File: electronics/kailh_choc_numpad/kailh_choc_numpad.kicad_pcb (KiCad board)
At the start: 2 copper layers, 10 x 10 mm, 18 parts

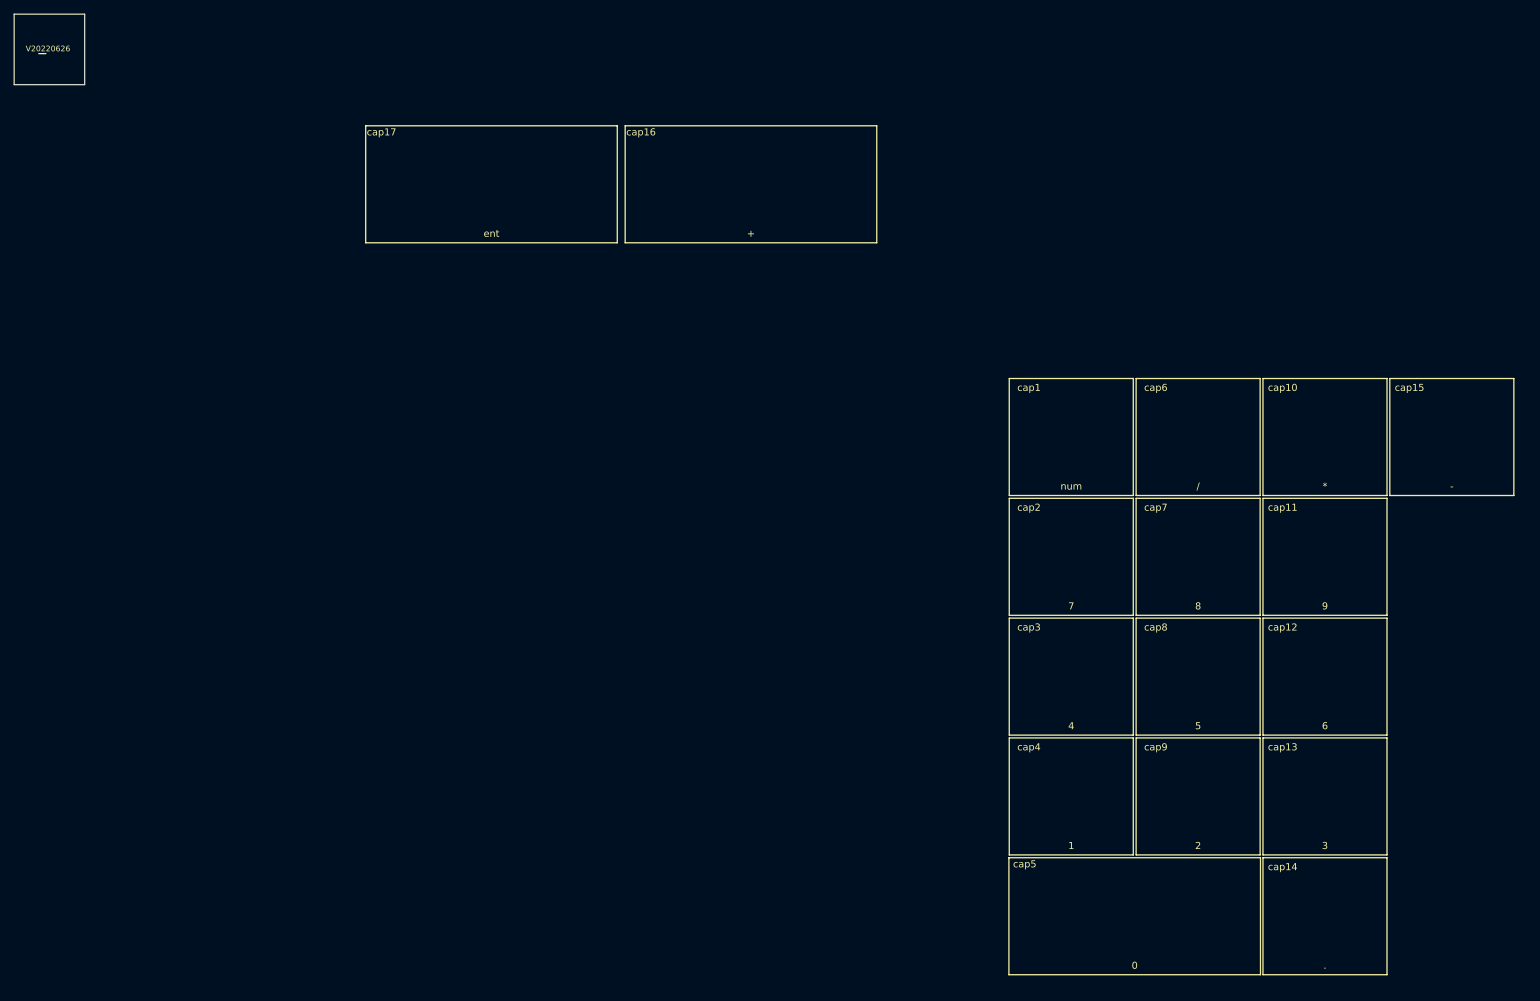
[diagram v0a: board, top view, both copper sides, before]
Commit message: placed keycaps
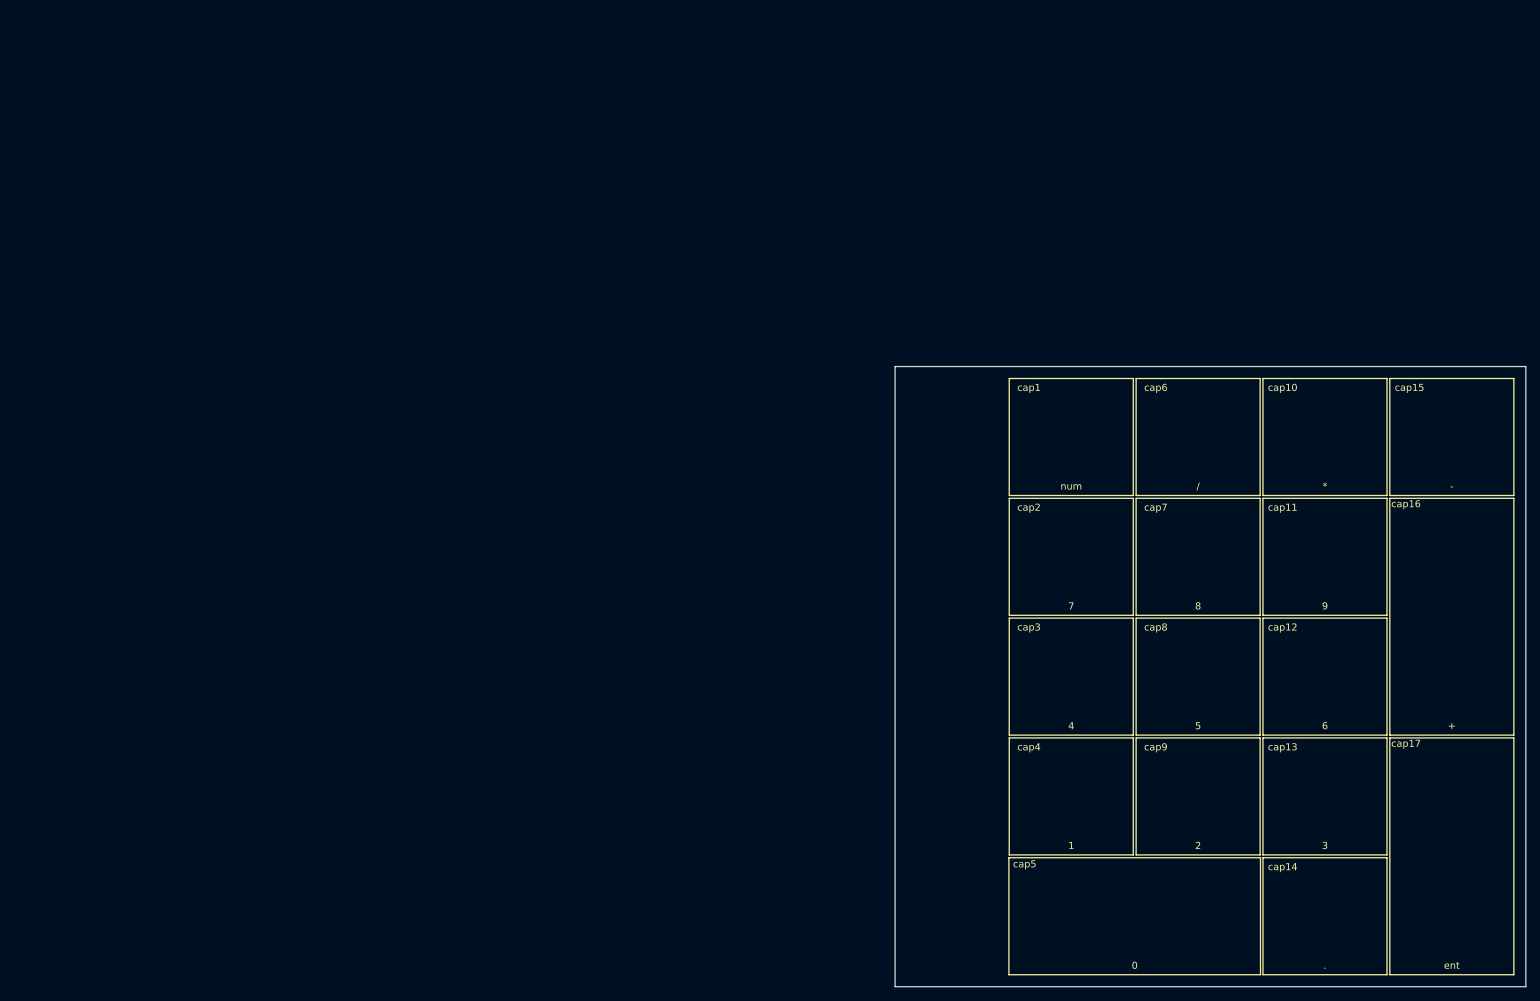
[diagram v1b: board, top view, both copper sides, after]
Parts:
- N1: moved to B.Cu
- cap16, cap17: footprint SquantorSwitches:KAILH_choc_keycap_2 -> SquantorSwitches:KAILH_choc_keycap_2_vertical
- cap5: footprint SquantorSwitches:KAILH_choc_keycap_2 -> SquantorSwitches:KAILH_choc_keycap_2_horizontal
- moved N1 227.3 mm to (224.5, 132.0), turned to 180 degrees
- moved cap17 166.3 mm to (224.0, 139.5)
- moved cap16 116.9 mm to (224.0, 105.5)
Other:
- board size 10 x 10 mm -> 89.5 x 88 mm

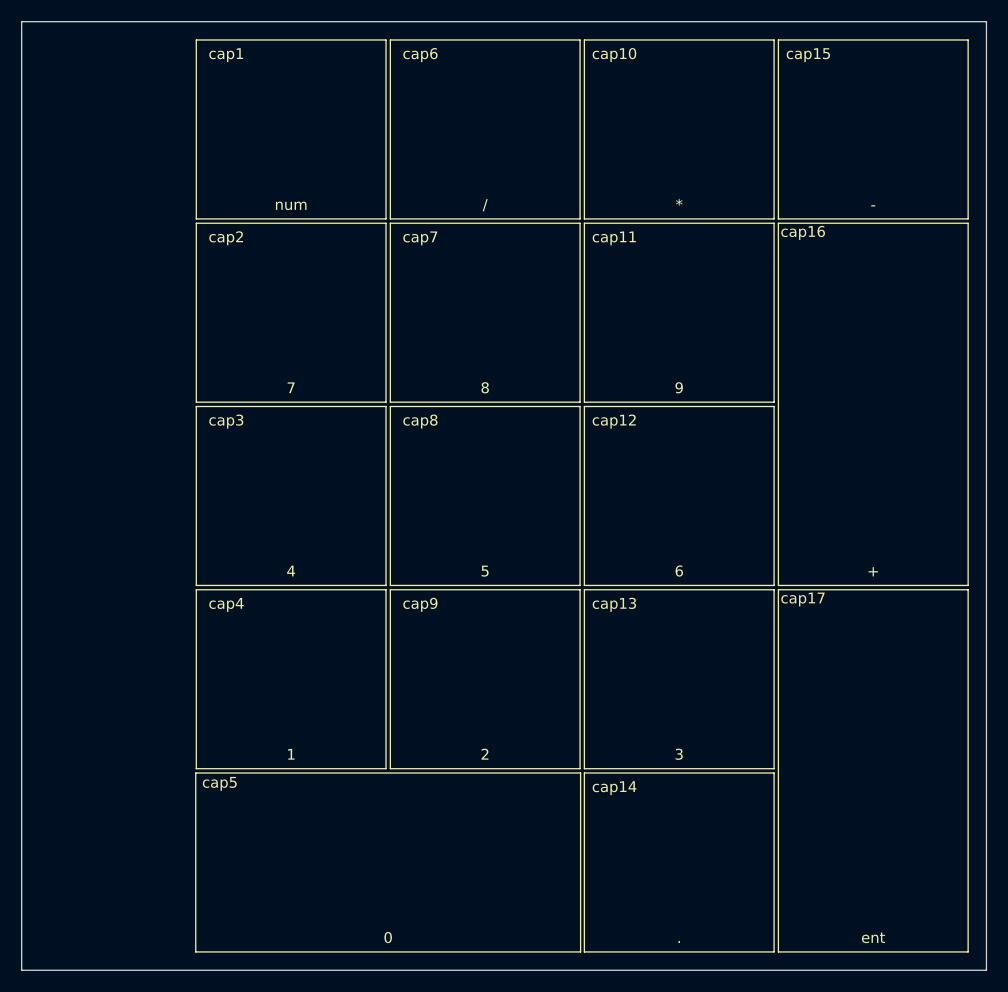
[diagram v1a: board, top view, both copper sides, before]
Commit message: placing and routing keyboard matrix
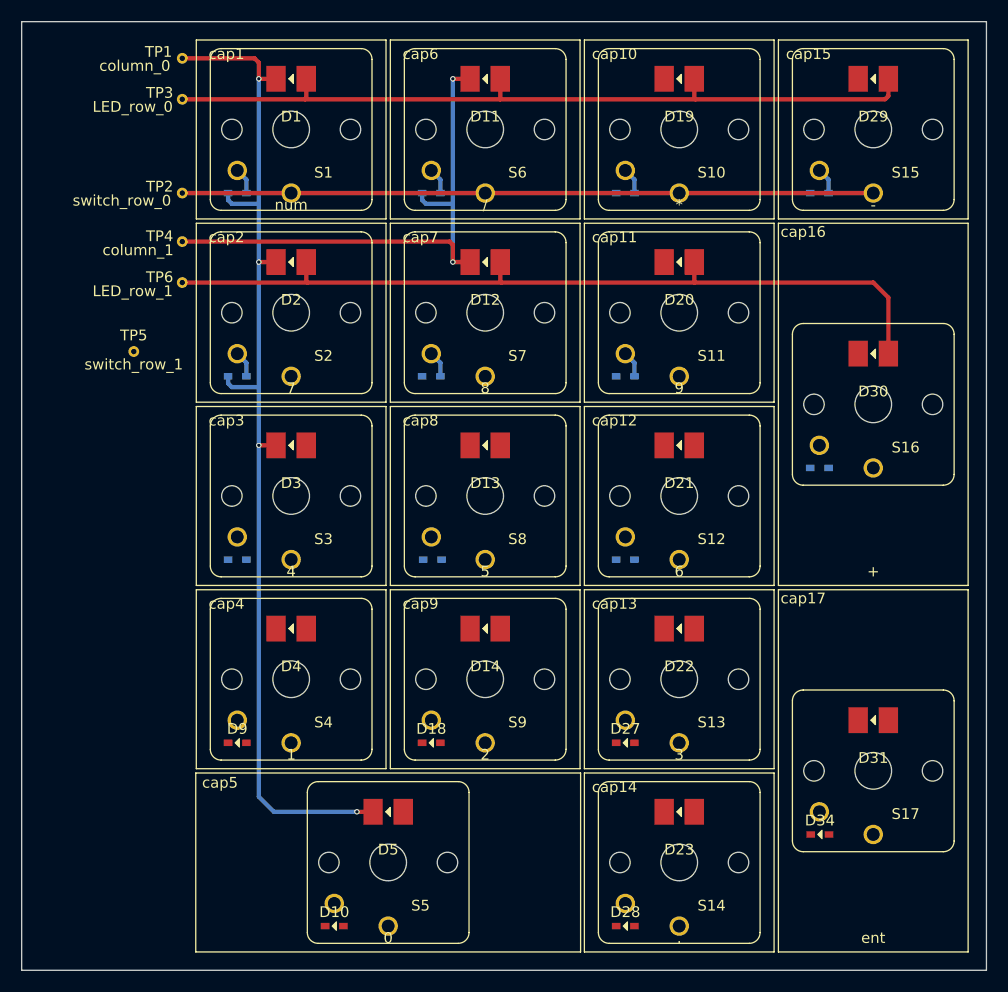
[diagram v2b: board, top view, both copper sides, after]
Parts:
- added D1: num, SquantorDiodes:LED_1208_0603, F.Cu at (170.0, 75.3)
- added D10: D, SquantorDiodes:SOD-523_hand, F.Cu at (174.0, 153.9)
- added D11: /, SquantorDiodes:LED_1208_0603, F.Cu at (188.0, 75.3)
- added D12: 8, SquantorDiodes:LED_1208_0603, F.Cu at (188.0, 92.3)
- added D13: 5, SquantorDiodes:LED_1208_0603, F.Cu at (188.0, 109.3)
- added D14: 2, SquantorDiodes:LED_1208_0603, F.Cu at (188.0, 126.3)
- added D15: D, SquantorDiodes:SOD-523_hand, B.Cu at (183.0, 85.9)
- added D16: D, SquantorDiodes:SOD-523_hand, B.Cu at (183.0, 102.9)
- added D17: D, SquantorDiodes:SOD-523_hand, B.Cu at (183.1, 119.9)
- added D18: D, SquantorDiodes:SOD-523_hand, F.Cu at (183.0, 136.9)
- added D19: *, SquantorDiodes:LED_1208_0603, F.Cu at (206.0, 75.3)
- added D2: 7, SquantorDiodes:LED_1208_0603, F.Cu at (170.0, 92.3)
- added D20: 9, SquantorDiodes:LED_1208_0603, F.Cu at (206.0, 92.3)
- added D21: 6, SquantorDiodes:LED_1208_0603, F.Cu at (206.0, 109.3)
- added D22: 3, SquantorDiodes:LED_1208_0603, F.Cu at (206.0, 126.3)
- added D23: ., SquantorDiodes:LED_1208_0603, F.Cu at (206.0, 143.3)
- added D24: D, SquantorDiodes:SOD-523_hand, B.Cu at (201.0, 85.9)
- added D25: D, SquantorDiodes:SOD-523_hand, B.Cu at (201.0, 102.9)
- added D26: D, SquantorDiodes:SOD-523_hand, B.Cu at (201.0, 119.9)
- added D27: D, SquantorDiodes:SOD-523_hand, F.Cu at (201.0, 136.9)
- added D28: D, SquantorDiodes:SOD-523_hand, F.Cu at (201.0, 153.9)
- added D29: -, SquantorDiodes:LED_1208_0603, F.Cu at (224.0, 75.3)
- added D3: 4, SquantorDiodes:LED_1208_0603, F.Cu at (170.0, 109.3)
- added D30: +, SquantorDiodes:LED_1208_0603, F.Cu at (224.0, 100.8)
- added D31: ent, SquantorDiodes:LED_1208_0603, F.Cu at (224.0, 134.8)
- added D32: D, SquantorDiodes:SOD-523_hand, B.Cu at (219.0, 85.9)
- added D33: D, SquantorDiodes:SOD-523_hand, B.Cu at (219.0, 111.4)
- added D34: D, SquantorDiodes:SOD-523_hand, F.Cu at (219.1, 145.4)
- added D4: 1, SquantorDiodes:LED_1208_0603, F.Cu at (170.0, 126.3)
- added D5: 0, SquantorDiodes:LED_1208_0603, F.Cu at (179.0, 143.3)
- added D6: D, SquantorDiodes:SOD-523_hand, B.Cu at (165.0, 85.9)
- added D7: D, SquantorDiodes:SOD-523_hand, B.Cu at (165.0, 102.9)
- added D8: D, SquantorDiodes:SOD-523_hand, B.Cu at (165.0, 119.9)
- added D9: D, SquantorDiodes:SOD-523_hand, F.Cu at (165.0, 136.9)
- added S1: num, SquantorSwitches:KAILH_choc_LED, F.Cu at (170.0, 80.0)
- added S10: *, SquantorSwitches:KAILH_choc_LED, F.Cu at (206.0, 80.0)
- added S11: 9, SquantorSwitches:KAILH_choc_LED, F.Cu at (206.0, 97.0)
- added S12: 6, SquantorSwitches:KAILH_choc_LED, F.Cu at (206.0, 114.0)
- added S13: 3, SquantorSwitches:KAILH_choc_LED, F.Cu at (206.0, 131.0)
- added S14: ., SquantorSwitches:KAILH_choc_LED, F.Cu at (206.0, 148.0)
- added S15: -, SquantorSwitches:KAILH_choc_LED, F.Cu at (224.0, 80.0)
- added S16: +, SquantorSwitches:KAILH_choc_LED, F.Cu at (224.0, 105.5)
- added S17: ent, SquantorSwitches:KAILH_choc_LED, F.Cu at (224.0, 139.5)
- added S2: 7, SquantorSwitches:KAILH_choc_LED, F.Cu at (170.0, 97.0)
- added S3: 4, SquantorSwitches:KAILH_choc_LED, F.Cu at (170.0, 114.0)
- added S4: 1, SquantorSwitches:KAILH_choc_LED, F.Cu at (170.0, 131.0)
- added S5: 0, SquantorSwitches:KAILH_choc_LED, F.Cu at (179.0, 148.0)
- added S6: /, SquantorSwitches:KAILH_choc_LED, F.Cu at (188.0, 80.0)
- added S7: 8, SquantorSwitches:KAILH_choc_LED, F.Cu at (188.0, 97.0)
- added S8: 5, SquantorSwitches:KAILH_choc_LED, F.Cu at (188.0, 114.0)
- added S9: 2, SquantorSwitches:KAILH_choc_LED, F.Cu at (188.0, 131.0)
- added TP1: column_0, SquantorTestPoints:TestPoint_hole_H05R10, F.Cu at (159.9, 73.4)
- added TP2: switch_row_0, SquantorTestPoints:TestPoint_hole_H05R10, F.Cu at (159.9, 85.9)
- added TP3: LED_row_0, SquantorTestPoints:TestPoint_hole_H05R10, F.Cu at (159.9, 77.2)
- added TP4: column_1, SquantorTestPoints:TestPoint_hole_H05R10, F.Cu at (159.9, 90.4)
- added TP5: switch_row_1, SquantorTestPoints:TestPoint_hole_H05R10, F.Cu at (155.4, 100.6)
- added TP6: LED_row_1, SquantorTestPoints:TestPoint_hole_H05R10, F.Cu at (159.9, 94.2)
- moved N1 75.1 mm to (153.0, 155.0)
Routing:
- net /column_0: track 0.00 -> 98.6 mm, vias 0 -> 4
- net /LED_row_1: track 0.00 -> 77.1 mm
- net /LED_row_0: track 0.00 -> 73.0 mm
- net /switch_row_0: track 0.00 -> 64.1 mm
- net /column_1: track 0.00 -> 50.7 mm, vias 0 -> 2
- net Net-(D7-Pad2): track 0.00 -> 2.45 mm
- net Net-(D6-Pad2): track 0.00 -> 2.45 mm
- net Net-(D32-Pad2): track 0.00 -> 2.45 mm
- net Net-(D25-Pad2): track 0.00 -> 2.45 mm
- net Net-(D24-Pad2): track 0.00 -> 2.45 mm
- net Net-(D16-Pad2): track 0.00 -> 2.45 mm
- net Net-(D15-Pad2): track 0.00 -> 2.45 mm

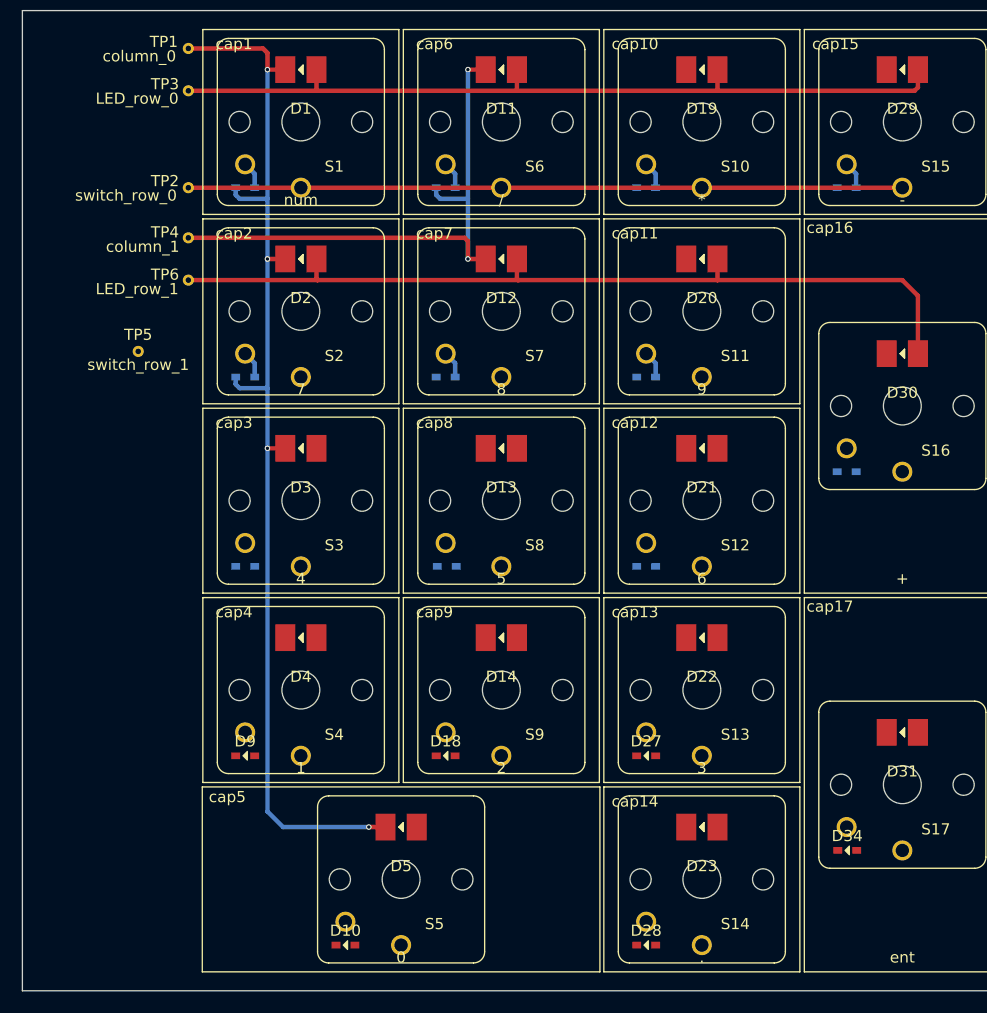
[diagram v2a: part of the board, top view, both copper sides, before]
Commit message: fully placed and routed switch matrix
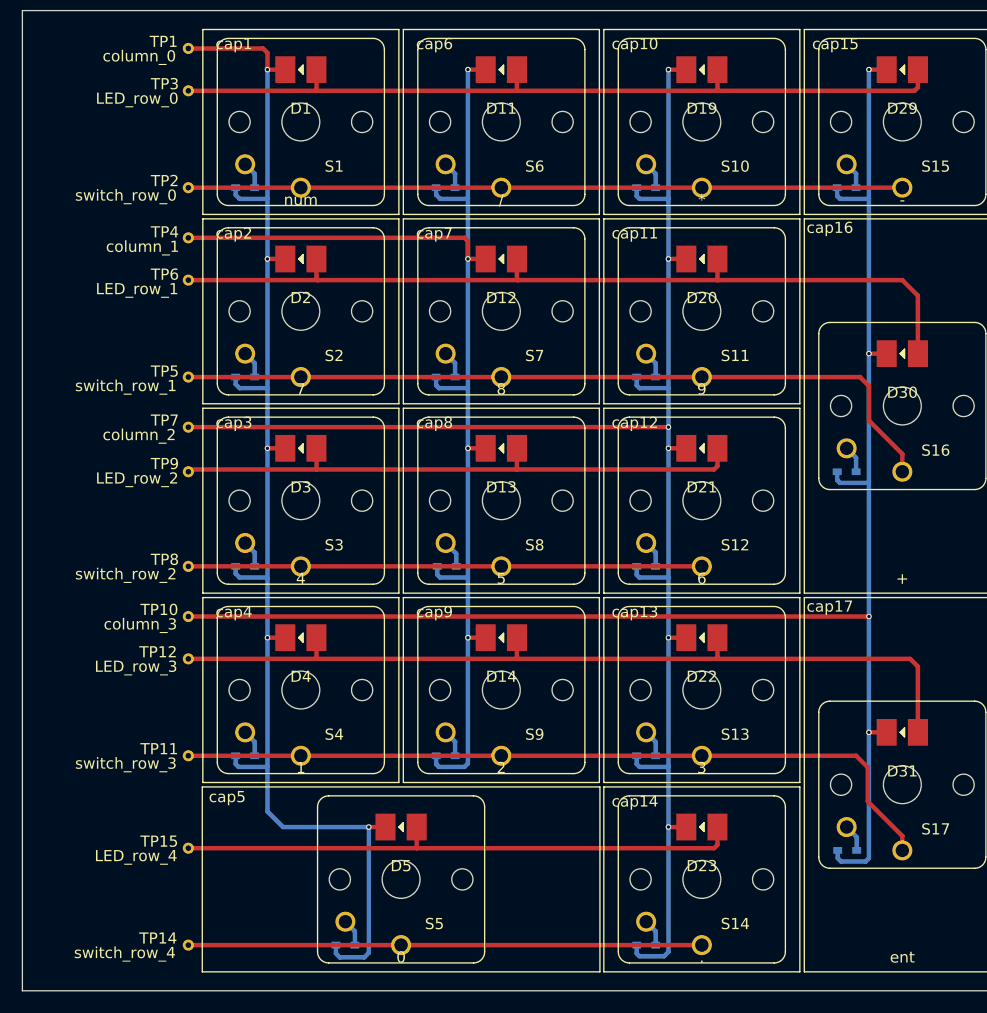
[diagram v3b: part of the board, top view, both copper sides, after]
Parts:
- added TP10: column_3, SquantorTestPoints:TestPoint_hole_H05R10, F.Cu at (159.9, 124.4)
- added TP11: switch_row_3, SquantorTestPoints:TestPoint_hole_H05R10, F.Cu at (159.9, 136.9)
- added TP12: LED_row_3, SquantorTestPoints:TestPoint_hole_H05R10, F.Cu at (159.9, 128.2)
- added TP14: switch_row_4, SquantorTestPoints:TestPoint_hole_H05R10, F.Cu at (159.9, 153.9)
- added TP15: LED_row_4, SquantorTestPoints:TestPoint_hole_H05R10, F.Cu at (159.9, 145.2)
- added TP7: column_2, SquantorTestPoints:TestPoint_hole_H05R10, F.Cu at (159.9, 107.4)
- added TP8: switch_row_2, SquantorTestPoints:TestPoint_hole_H05R10, F.Cu at (159.9, 119.9)
- added TP9: LED_row_2, SquantorTestPoints:TestPoint_hole_H05R10, F.Cu at (159.9, 111.4)
- D10, D18, D27, D28, D34, D9: moved to B.Cu
- moved TP5 5.05 mm to (159.9, 102.9)
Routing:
- net /column_2: track 0.00 -> 149.0 mm, vias 0 -> 6
- net /column_3: track 0.00 -> 147.9 mm, vias 0 -> 4
- net /LED_row_3: track 0.00 -> 77.4 mm
- net /switch_row_1: track 0.00 -> 70.4 mm
- net /switch_row_3: track 0.00 -> 70.2 mm
- net /column_1: track 50.7 -> 110.3 mm, vias 2 -> 4
- net /LED_row_2: track 0.00 -> 53.1 mm
- net /LED_row_4: track 0.00 -> 51.1 mm
- net /switch_row_4: track 0.00 -> 46.1 mm
- net /switch_row_2: track 0.00 -> 46.1 mm
- net /column_0: track 98.6 -> 122.9 mm, vias 4 -> 5
- net Net-(D17-Pad2): track 0.00 -> 2.49 mm
- net Net-(D34-Pad2): track 0.00 -> 2.47 mm
- net Net-(D8-Pad2): track 0.00 -> 2.45 mm
- net Net-(D33-Pad2): track 0.00 -> 2.45 mm
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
